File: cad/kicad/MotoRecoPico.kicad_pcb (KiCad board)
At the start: 4 copper layers, 21 x 61 mm, 41 parts, among them J1 1-967658-1, J2 DM3AT-SF-PEJM5, J3 GT-502MGG-N, Q1 MMBT3904, Q2 ZXMP6A17E6Q, U2 MCP25625, U3 Pico 2, U4 AP63205WU-7, Y1 16MHz

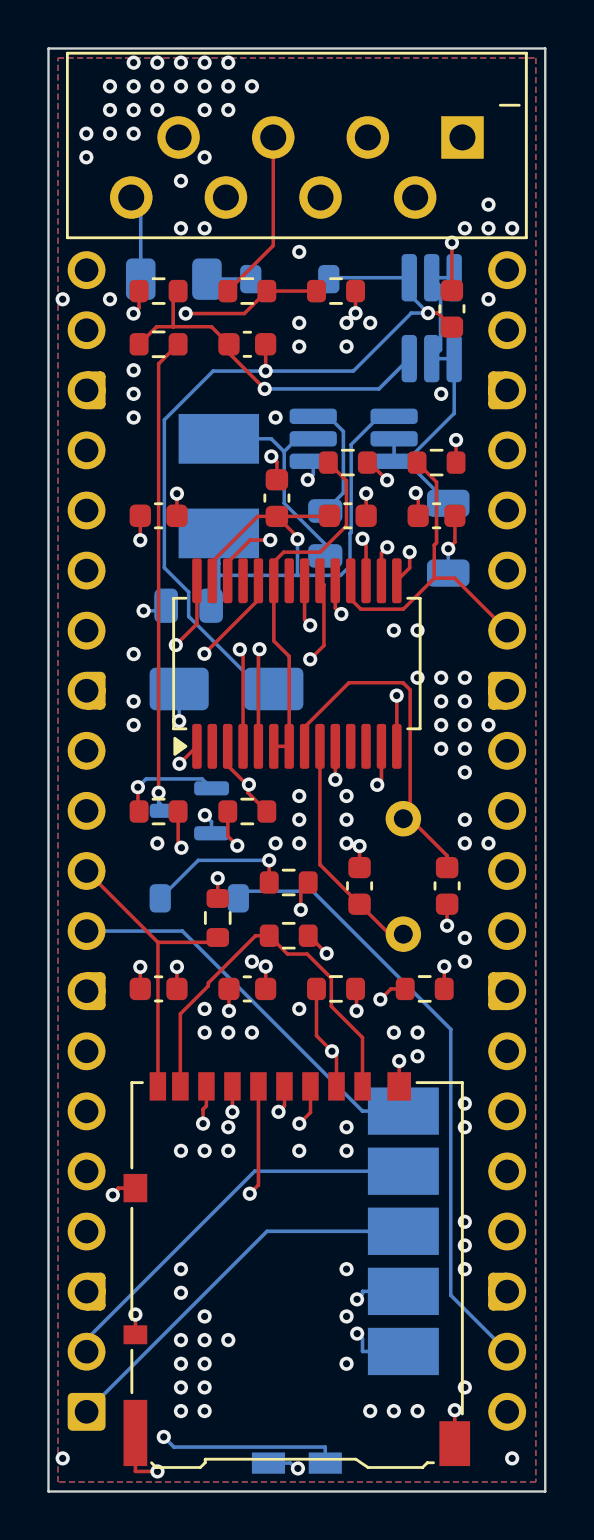
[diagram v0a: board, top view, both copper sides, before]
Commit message: Add the v5 JLCPCB-assembly board variant (MRP_ASSY=jlc) with J4 direct-wire pads
Board and schematic are now the v5 build: all 37 machine-placed SMT parts on
the top face, the Pico soldered flush to the bottom face via castellations
(custom Pico2-SMD-Flush footprint), GPS off the board (wired straight to the
Pico), Q2 -> SI2309, Y1 -> 3225 SMD, chips 0603 to stay on HASL.

J4 adds five bare solder pads between J1 and the board edge on the Pico face
for wiring the vehicle loom directly: L H I G V (CANL, CANH, IGN, GND, +12V
upstream of F1) in the same left-to-right order as the J1 pins they tap, so
ses_import draws the five escapes straight from the J1 barrels on B.Cu with
no vias; dsn_export hides J4 and its lanes from the autorouter.

Freerouting is now 2.5.0: try_thermal's parser and -mp follow the new CLI,
xtal_check tolerates the fanout vias, and two new gates reject bad seeds
(plane_gate.py for In1 GND fragments, drc_detail.py prints what DRC hit).
jlc_top.py writes the top-face-only BOM/CPL pair for the assembly order, and
docs/datasheets holds the vendor PDFs behind the polarity check.

Co-Authored-By: Claude Fable 5 <noreply@anthropic.com>
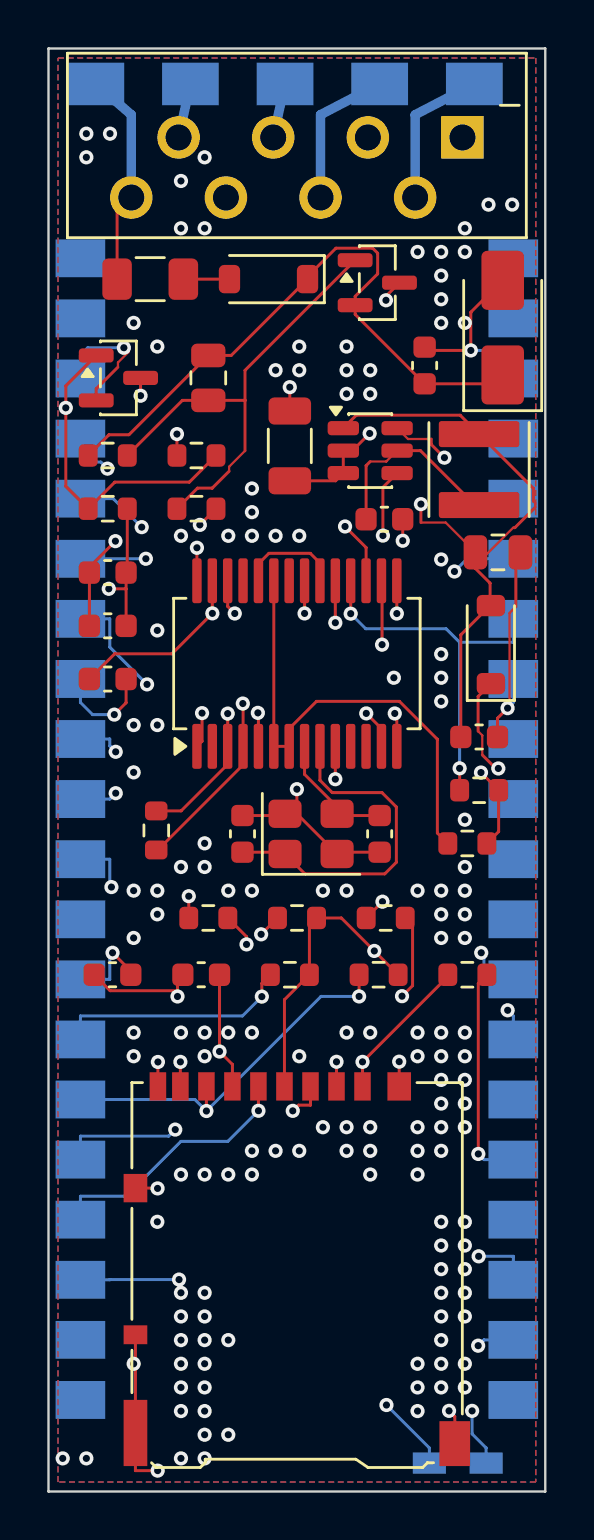
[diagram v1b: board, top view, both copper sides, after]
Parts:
- removed J3: GT-502MGG-N, GPS-5P-SMD-2.54
- added J4: DIRECT-WIRE, PAD-5P-DIRECT, B.Cu at (10.0, 1.50)
- C13: footprint C_0603_1608Metric -> C_0805_2012Metric
- C14, C15, D1, D2, D3, F1, Q1: moved to F.Cu
- C16: footprint C_0805_2012Metric -> C_0603_1608Metric; moved to F.Cu
- C7, C8: value 22pF -> 12pF
- L1: footprint L_4030_HandSolder -> L_Abracon_ASPI-4030S; moved to F.Cu
- Q2: value ZXMP6A17E6Q -> SI2309; footprint TSOT-23-6_HandSoldering -> SOT-23; moved to F.Cu
- U3: footprint RaspberryPi_Pico_Common_THT -> Pico2-SMD-Flush
- U4: footprint TSOT-23-6_HandSoldering -> TSOT-23-6; moved to F.Cu
- Y1: footprint Crystal_HC49-4H_Vertical -> Crystal_SMD_3225-4Pin_3.2x2.5mm; moved to F.Cu
- moved U3 26.2 mm to (10.5, 33.0)
- moved D2 19.2 mm to (19.2, 11.8), turned to 90 degrees
- moved Q1 18.5 mm to (2.96, 13.9), turned to 0 degrees
- moved R7 16.9 mm to (17.7, 33.6)
- moved D3 16.3 mm to (18.7, 25.2), turned to 90 degrees
- moved C4 14.7 mm to (2.50, 24.4)
- moved R6 14.0 mm to (18.2, 31.4)
- moved R4 13.3 mm to (2.50, 19.5)
- moved C15 13.3 mm to (19.0, 21.3), turned to 0 degrees
- moved C6 13.2 mm to (18.2, 29.1), turned to 0 degrees
- moved C5 12.3 mm to (2.50, 26.7)
- moved L1 11.0 mm to (18.2, 17.8), turned to 90 degrees
- moved C14 7.75 mm to (10.2, 16.8), turned to 90 degrees
- moved R12 7.73 mm to (17.7, 39.2)
- moved R1 7.27 mm to (2.50, 17.2)
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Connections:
- Q2 pad 1: V12_SW -> Q2_G
- Q2 pad 2: V12_SW -> V12P
- Q2 pad 3: Q2_G -> V12_SW
- U3 pad 1: GPS_TX -> (no net)
- U3 pad 2: GPS_RX -> (no net)
- U3 pad 9: GPS_PPS -> (no net)
- Y1 pad 2: XTAL2 -> GND
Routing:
- net GND: track 30.9 -> 78.4 mm, vias 137 -> 160
- net V3V3: track 16.1 -> 37.1 mm, vias 14 -> 7
- net GPS_RX: track 16.9 -> 0.00 mm
- net GPS_TX: track 16.6 -> 0.00 mm
- net GPS_PPS: track 16.5 -> 0.00 mm
- net V5: track 47.2 -> 63.2 mm, vias 2 -> 3
- net V12P: track 41.9 -> 26.6 mm, vias 3 -> 0
- net CANL: track 31.2 -> 43.6 mm
- net Q1_C: track 20.2 -> 8.22 mm, vias 1 -> 2
- net IG_RAW: track 7.29 -> 17.4 mm, vias 0 -> 1
- net XTAL2: track 14.6 -> 5.25 mm
- net TXCAN: track 12.4 -> 4.42 mm, vias 2 -> 0
- net LED_STATUS: track 35.5 -> 42.8 mm, vias 1 -> 2
- net Q1_B: track 31.3 -> 37.5 mm
- net V12_RAW: track 3.62 -> 9.18 mm
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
